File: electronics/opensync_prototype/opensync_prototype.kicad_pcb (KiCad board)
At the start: 4 copper layers, 155 x 100 mm, 107 parts, among them J1 61400416121, J10 61611042121502, J11 61611042121502, J2 61611042121502, J4 61611042121502, J5 61611042121502, J6 61611042121502, J7 61611042121502, J8 61611042121502, J9 61611042121502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

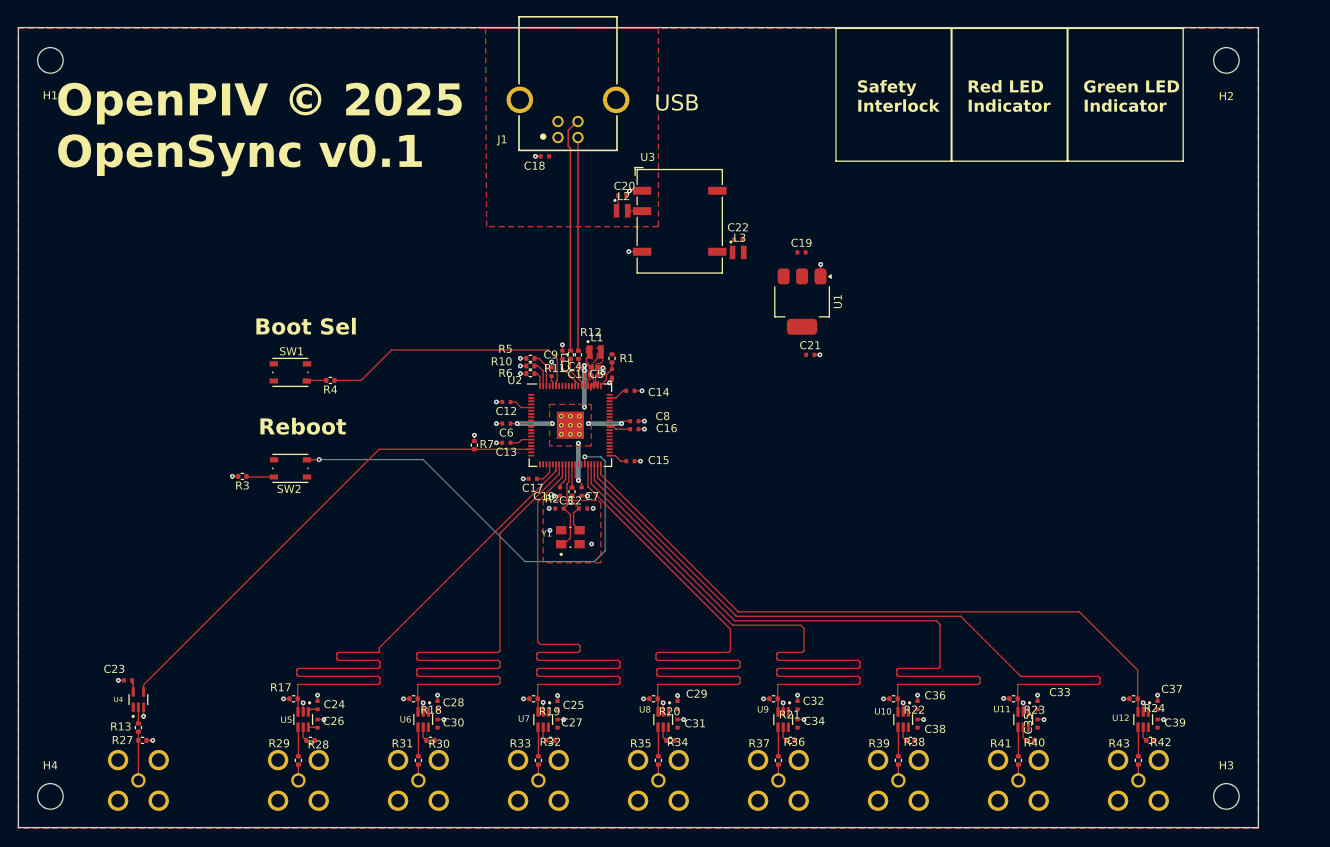
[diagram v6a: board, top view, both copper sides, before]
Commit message: Fixed all DRC violations
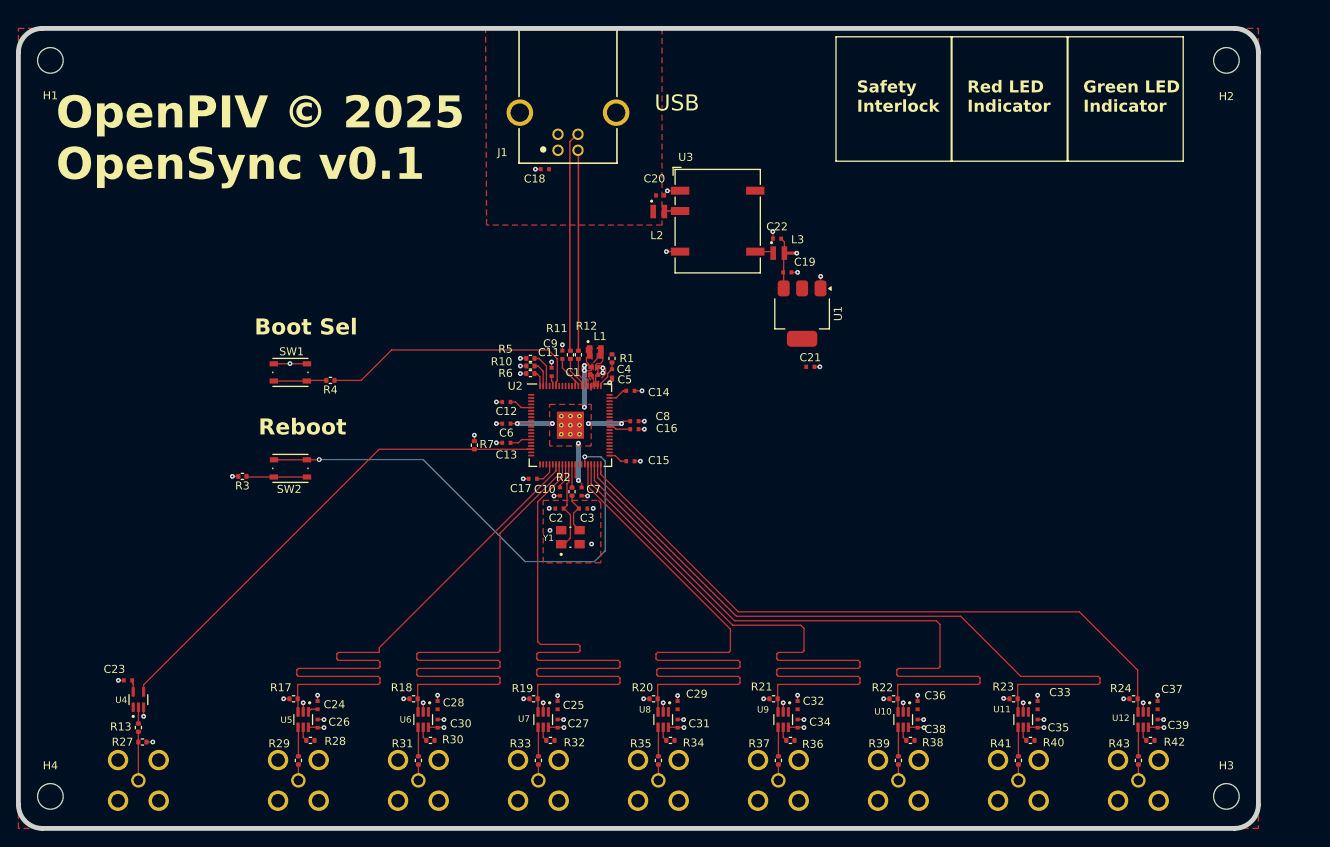
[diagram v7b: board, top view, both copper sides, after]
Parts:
- moved L3 5.08 mm to (157.0, 73.1)
- moved C22 4.87 mm to (156.8, 71.3)
- moved C20 4.75 mm to (142.2, 65.9)
- moved U3 4.75 mm to (149.4, 70.4)
- moved L2 4.58 mm to (142.0, 67.9)
- moved C19 3.07 mm to (158.1, 75.5)
- moved C18 1.60 mm to (127.8, 62.6)
- moved J1 1.60 mm to (130.7, 53.5)
- moved C21 1.50 mm to (161.0, 87.3)
- moved U1 1.50 mm to (160.0, 80.7)
- moved R27 0.20 mm to (77.5, 134.2)
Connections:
- C2 pad 1: Net-(C2-Pad1) -> GND
- C3 pad 1: Net-(C2-Pad1) -> GND
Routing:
- net +5V: track 1.17 -> 23.7 mm, vias 0 -> 9
- net GND: track 47.0 -> 52.9 mm, vias 62 -> 65
- net Net-(R3-Pad1): track 3.45 -> 7.60 mm
- net Net-(R4-Pad2): track 2.47 -> 6.60 mm
- net /Microcontroller and Ext. Clock/RUN: track 58.1 -> 62.2 mm
- net Net-(U3-+VOUT): track 0.00 -> 3.14 mm
- net VBUS: track 2.03 -> 0.00 mm
- net /Power and Data/USB_D-: track 27.1 -> 25.2 mm
- net /Power and Data/USB_D+: track 29.1 -> 27.6 mm
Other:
- outline, holes or cut-outs redrawn

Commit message: PCB touch-ups
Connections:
- net /Microcontroller and Ext. Clock/QSPL_SS renamed /Microcontroller and Ext. Clock/QSPI_SS
- U2 pad 70: unconnected-(U2-QSPI_SD3-Pad70) -> /Microcontroller and Ext. Clock/QSPI_SD3
- U2 pad 71: unconnected-(U2-QSPI_SCLK-Pad71) -> /Microcontroller and Ext. Clock/QSPI_SCLK
- U2 pad 72: unconnected-(U2-QSPI_SD0-Pad72) -> /Microcontroller and Ext. Clock/QSPI_SD0
- U2 pad 73: unconnected-(U2-QSPI_SD2-Pad73) -> /Microcontroller and Ext. Clock/QSPI_SD2
- U2 pad 74: unconnected-(U2-QSPI_SD1-Pad74) -> /Microcontroller and Ext. Clock/QSPI_SD1
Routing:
- net +3V3: track 28.5 -> 37.5 mm
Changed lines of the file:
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@@
 	(net 24 "Net-(R3-Pad1)")
 	(net 25 "Net-(R4-Pad2)")
-	(net 26 "/Microcontroller and Ext. Clock/QSPL_SS")
+	(net 26 "/Microcontroller and Ext. Clock/QSPI_SS")
 	(net 27 "/Microcontroller and Ext. Clock/CLOCK_1")
 	(net 28 "/Microcontroller and Ext. Clock/CLOCK_3")
@@
 	(net 53 "unconnected-(U2-GPIO47_ADC7-Pad58)")
 	(net 54 "unconnected-(U2-GPIO33-Pad42)")
-	(net 55 "unconnected-(U2-QSPI_SD1-Pad74)")
+	(net 55 "/Microcontroller and Ext. Clock/QSPI_SD1")
 	(net 56 "unconnected-(U2-GPIO46_ADC6-Pad57)")
 	(net 57 "unconnected-(U2-GPIO40_ADC0-Pad49)")
-	(net 58 "unconnected-(U2-QSPI_SD3-Pad70)")
-	(net 59 "unconnected-(U2-QSPI_SD2-Pad73)")
-	(net 60 "unconnected-(U2-QSPI_SD0-Pad72)")
+	(net 58 "/Microcontroller and Ext. Clock/QSPI_SD3")
+	(net 59 "/Microcontroller and Ext. Clock/QSPI_SD2")
+	(net 60 "/Microcontroller and Ext. Clock/QSPI_SD0")
 	(net 61 "unconnected-(U2-GPIO35-Pad44)")
 	(net 62 "unconnected-(U2-GPIO45_ADC5-Pad56)")
@@
 	(net 65 "unconnected-(U2-GPIO42_ADC2-Pad53)")
 	(net 66 "unconnected-(U2-GPIO7-Pad4)")
-	(net 67 "unconnected-(U2-QSPI_SCLK-Pad71)")
+	(net 67 "/Microcontroller and Ext. Clock/QSPI_SCLK")
 	(net 68 "unconnected-(U2-SWCLK-Pad33)")
 	(net 69 "unconnected-(U2-GPIO36-Pad45)")
@@
 			(layers "F.Cu" "F.Mask" "F.Paste")
 			(roundrect_rratio 0.25)
-			(net 26 "/Microcontroller and Ext. Clock/QSPL_SS")
+			(net 26 "/Microcontroller and Ext. Clock/QSPI_SS")
 			(pintype "passive")
 		)
@@
 			)
 		)
+		(property "DigiKey_Part_Number" "296-11934-1-ND"
+			(at 0 0 90)
+			(unlocked yes)
+			(layer "F.Fab")
+			(hide yes)
+			(effects
+				(font
+					(size 1 1)
+					(thickness 0.15)
+				)
+			)
+		)
+		(property "SnapEDA_Link" "https://www.snapeda.com/parts/SN74LVC1G17DCKR/Texas+Instruments/view-part/?ref=snap"
+			(at 0 0 90)
+			(unlocked yes)
+			(layer "F.Fab")
+			(hide yes)
+			(effects
+				(font
+					(size 1 1)
+					(thickness 0.15)
+				)
+			)
+		)
+		(property "Description_1" "Single 1.65-V to 5.5-V buffer with Schmitt-Trigger inputs"
+			(at 0 0 90)
+			(unlocked yes)
+			(layer "F.Fab")
+			(hide yes)
+			(effects
+				(font
+					(size 1 1)
+					(thickness 0.15)
+				)
+			)
+		)
+		(property "MF" "Texas Instruments"
+			(at 0 0 90)
+			(unlocked yes)
+			(layer "F.Fab")
+			(hide yes)
+			(effects
+				(font
+					(size 1 1)
+					(thickness 0.15)
+				)
+			)
+		)
+		(property "Package" "SC70-5 Texas Instruments"
+			(at 0 0 90)
+			(unlocked yes)
+			(layer "F.Fab")
+			(hide yes)
+			(effects
+				(font
+					(size 1 1)
+					(thickness 0.15)
+				)
+			)
+		)
+		(property "Check_prices" "https://www.snapeda.com/parts/SN74LVC1G17DCKR/Texas+Instruments/view-part/?ref=eda"
+			(at 0 0 90)
+			(unlocked yes)
+			(layer "F.Fab")
+			(hide yes)
+			(effects
+				(font
+					(size 1 1)
+					(thickness 0.15)
+				)
+			)
+		)
+		(property "MP" "SN74LVC1G17DCKR"
+			(at 0 0 90)
+			(unlocked yes)
+			(layer "F.Fab")
+			(hide yes)
+			(effects
+				(font
+					(size 1 1)
+					(thickness 0.15)
+				)
+			)
+		)
 		(sheetname "/Input Ports/")
 		(sheetfile "input_ports.kicad_sch")
@@
 			(layers "F.Cu" "F.Mask" "F.Paste")
 			(roundrect_rratio 0.25)
-			(net 58 "unconnected-(U2-QSPI_SD3-Pad70)")
+			(net 58 "/Microcontroller and Ext. Clock/QSPI_SD3")
 			(pinfunction "QSPI_SD3")
 			(pintype "bidirectional+no_connect")
@@
 			(layers "F.Cu" "F.Mask" "F.Paste")
 			(roundrect_rratio 0.25)
-			(net 67 "unconnected-(U2-QSPI_SCLK-Pad71)")
+			(net 67 "/Microcontroller and Ext. Clock/QSPI_SCLK")
 			(pinfunction "QSPI_SCLK")
 			(pintype "output+no_connect")
@@
 			(layers "F.Cu" "F.Mask" "F.Paste")
 			(roundrect_rratio 0.25)
-			(net 60 "unconnected-(U2-QSPI_SD0-Pad72)")
+			(net 60 "/Microcontroller and Ext. Clock/QSPI_SD0")
 			(pinfunction "QSPI_SD0")
 			(pintype "bidirectional+no_connect")
@@
 			(layers "F.Cu" "F.Mask" "F.Paste")
 			(roundrect_rratio 0.25)
-			(net 59 "unconnected-(U2-QSPI_SD2-Pad73)")
+			(net 59 "/Microcontroller and Ext. Clock/QSPI_SD2")
 			(pinfunction "QSPI_SD2")
 			(pintype "bidirectional+no_connect")
@@
 			(layers "F.Cu" "F.Mask" "F.Paste")
 			(roundrect_rratio 0.25)
-			(net 55 "unconnected-(U2-QSPI_SD1-Pad74)")
+			(net 55 "/Microcontroller and Ext. Clock/QSPI_SD1")
 			(pinfunction "QSPI_SD1")
 			(pintype "bidirectional+no_connect")
@@
 			(layers "F.Cu" "F.Mask" "F.Paste")
 			(roundrect_rratio 0.25)
-			(net 26 "/Microcontroller and Ext. Clock/QSPL_SS")
+			(net 26 "/Microcontroller and Ext. Clock/QSPI_SS")
 			(pinfunction "QSPI_SS")
 			(pintype "bidirectional")
@@
 	)
 	(segment
+		(start 174.4 130.115)
+		(end 173.575 130.115)
+		(width 0.1565)
+		(layer "F.Cu")
+		(net 1)
+	)
+	(segment
+		(start 113.575 130.115)
+		(end 113.25 130.44)
+		(width 0.1565)
+		(layer "F.Cu")
+		(net 1)
+	)
+	(segment
 		(start 128.65 88.465)
 		(end 128.65 89.058516)
@@
 	)
 	(segment
+		(start 143.575 130.115)
+		(end 143.25 130.44)
+		(width 0.1565)
+		(layer "F.Cu")
+		(net 1)
+	)
+	(segment
 		(start 98.25 130.44)
 		(end 98.59 130.1)
@@
 	)
 	(segment
+		(start 144.4 130.115)
+		(end 143.575 130.115)
+		(width 0.1565)
+		(layer "F.Cu")
+		(net 1)
+	)
+	(segment
 		(start 136.391484 94.8)
 		(end 135.8965 94.8)
@@
 	)
 	(segment
+		(start 158.575 130.115)
+		(end 158.25 130.44)
+		(width 0.1565)
+		(layer "F.Cu")
+		(net 1)
+	)
+	(segment
 		(start 128.4 100.5)
 		(end 128.4 99.4965)
@@
 	)
 	(segment
+		(start 159.4 130.115)
+		(end 158.575 130.115)
+		(width 0.1565)
+		(layer "F.Cu")
+		(net 1)
+	)
+	(segment
 		(start 136.691484 95.1)
 		(end 136.391484 94.8)
@@
 	)
 	(segment
+		(start 129.4 130.115)
+		(end 128.575 130.115)
+		(width 0.1565)
+		(layer "F.Cu")
+		(net 1)
+	)
+	(segment
 		(start 124.15 91.7)
 		(end 124.85 92.4)
@@
 	)
 	(segment
+		(start 204.4 130.115)
+		(end 203.575 130.115)
+		(width 0.1565)
+		(layer "F.Cu")
+		(net 1)
+	)
+	(segment
 		(start 131.989 89.439)
 		(end 131.989 89.6925)
@@
 	)
 	(segment
+		(start 114.4 130.115)
+		(end 113.575 130.115)
+		(width 0.1565)
+		(layer "F.Cu")
+		(net 1)
+	)
+	(segment
 		(start 128.8 89.208516)
 		(end 128.8 89.7035)
@@
 	)
 	(segment
+		(start 188.575 130.115)
+		(end 188.25 130.44)
+		(width 0.1565)
+		(layer "F.Cu")
+		(net 1)
+	)
+	(segment
 		(start 137.6 90.3)
 		(end 136.711 91.189)
@@
 	)
 	(segment
+		(start 128.575 130.115)
+		(end 128.25 130.44)
+		(width 0.1565)
+		(layer "F.Cu")
+		(net 1)
+	)
+	(segment
 		(start 76.35 126.935)
 		(end 76.215 126.8)
@@
 	)
 	(segment
+		(start 203.575 130.115)
+		(end 203.25 130.44)
+		(width 0.1565)
+		(layer "F.Cu")
+		(net 1)
+	)
+	(segment
 		(start 99.385 130.1)
 		(end 99.4 130.115)
@@
 	)
 	(segment
+		(start 189.4 130.115)
+		(end 188.575 130.115)
+		(width 0.1565)
+		(layer "F.Cu")
+		(net 1)
+	)
+	(segment
 		(start 124.85 92.4)
 		(end 126.1035 92.4)
@@
 	)
 	(segment
+		(start 173.575 130.115)
+		(end 173.25 130.44)
+		(width 0.1565)
+		(layer "F.Cu")
+		(net 1)
+	)
+	(segment
 		(start 128.65 87.435)
 		(end 128.65 86.7)
@@
 		(start 157.7475 73.085)
 		(end 159.2475 73.085)
-		(width 0.4)
+		(width 0.3)
 		(layer "F.Cu")
 		(net 9)
@@
 		(start 157.6625 77.5)
 		(end 157.6625 73.17)
-		(width 0.1565)
+		(width 0.3)
 		(layer "F.Cu")
 		(net 9)
@@
 		(priority 3)
 		(connect_pads
-			(clearance 0.25)
+			(clearance 0.3)
 		)
 		(min_thickness 0.25)
